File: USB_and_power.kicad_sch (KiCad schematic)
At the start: 48 parts, among them J5 USB_C_Receptacle_USB2.0_14P, SW1 ResetButton, U3 LM2594M-3.3, U4 FT4232H, U5 93LC54B, Y1 ABLS7M2-12.000MHZ-D2Y-T

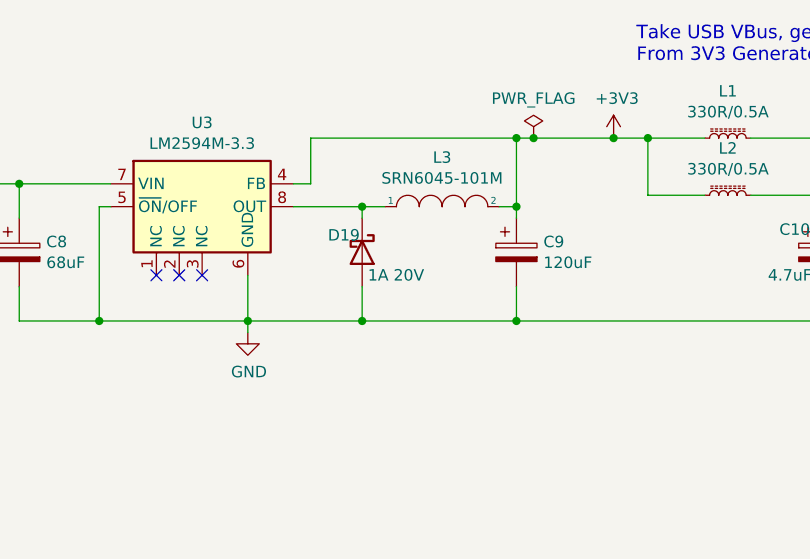
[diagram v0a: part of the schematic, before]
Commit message: BOM updates. Things needed changing due to availability
Tant Caps
Schotkey diodes
Pushbutton Switch

Signed-off-by: Marc Kelly <mpkelly@achenar.co.uk>
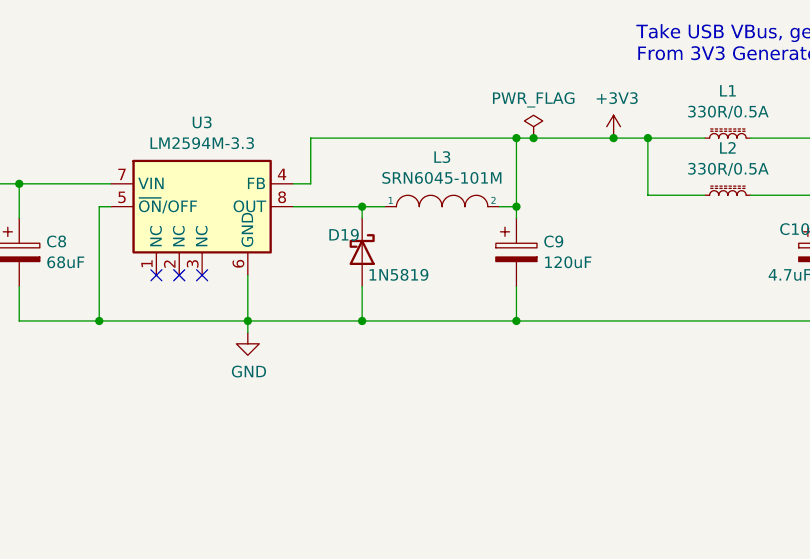
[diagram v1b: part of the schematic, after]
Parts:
- C10, C12: MFN Kyocera AVX -> Murata; MFP F981C475MMA -> GRM188R61E475KE11D; SUPPLIER_LINK https://www.mouser.co.uk/ProductDetail/Kyocera-AVX/F981C475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 -> https://eu.mouser.com/ProductDetail/Murata-Electronics/GRM1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; SUPPLIER_PN 647-F981C475MMA -> 81-GRM188R61E475KE1D
- D19: value 1A 20V -> 1N5819; MFN MCC -> Diodes Inc; MFP MBRX120LF-TP -> 1N5819HW-7-F; SUPPLIER_LINK https://www.mouser.co.uk/ProductDetail/Micro-Commercial-Com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 -> (none); SUPPLIER_PN 833-MBRX120LF-TP -> 621-1N5819HW-F
- SW1: SUPPLIER Farnell -> Mouser; SUPPLIER_PN 4715649 -> 640-SWT0110020016SSA
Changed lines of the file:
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@@
 			)
 		)
-		(property "Value" "1A 20V"
+		(property "Value" "1N5819"
 			(at 122.555 96.393 90)
 			(show_name no)
@@
 			)
 		)
-		(property "Datasheet" ""
+		(property "Datasheet" "https://4donline.ihs.com/images/VipMasterIC/IC/DIOD/DIOD-S-A0011437026/DIOD-S-A0011683586-1.pdf?hkey=CECEF36DEECDED6468708AAF2E19C0C6"
 			(at 121.92 93.853 0)
 			(hide yes)
@@
 			)
 		)
-		(property "MFN" "MCC"
+		(property "MFN" "Diodes Inc"
 			(at 121.92 93.853 0)
 			(hide yes)
@@
 			)
 		)
-		(property "MFP" "MBRX120LF-TP"
+		(property "MFP" "1N5819HW-7-F"
 			(at 121.92 93.853 0)
 			(hide yes)
@@
 			)
 		)
-		(property "SUPPLIER_LINK" "https://www.mouser.co.uk/ProductDetail/Micro-Commercial-Components-MCC/MBRX120LF-TP?qs=SdqRYZZ9IxC6ZMQgVhMv%2FA%3D%3D"
+		(property "SUPPLIER_PN" "621-1N5819HW-F"
+			(at 121.92 93.853 0)
+			(hide yes)
+			(show_name no)
+			(do_not_autoplace no)
+			(effects
+				(font
+					(size 1.27 1.27)
+				)
+			)
+		)
+		(property "ALT_SUPPLIER" ""
 			(at 121.92 93.853 0)
 			(hide yes)
@@
 			)
 		)
-		(property "SUPPLIER_PN" "833-MBRX120LF-TP"
+		(property "ALT_SUPPLIER_PN" ""
+			(at 121.92 93.853 0)
+			(hide yes)
+			(show_name no)
+			(do_not_autoplace no)
+			(effects
+				(font
+					(size 1.27 1.27)
+				)
+			)
+		)
+		(property "ALT_SUPPLIER_LINK" ""
+			(at 121.92 93.853 0)
+			(hide yes)
+			(show_name no)
+			(do_not_autoplace no)
+			(effects
+				(font
+					(size 1.27 1.27)
+				)
+			)
+		)
+		(property "SUPPLIER_LINK" ""
 			(at 121.92 93.853 0)
 			(hide yes)
@@
 			)
 		)
-		(property "Datasheet" ""
+		(property "Datasheet" "https://eu.mouser.com/datasheet/3/76/2/GRM188R61E475KE11_01A.pdf"
 			(at 172.72 93.853 0)
 			(hide yes)
@@
 			)
 		)
-		(property "MFN" "Kyocera AVX"
+		(property "MFN" "Murata"
 			(at 172.72 93.853 0)
 			(hide yes)
@@
 			)
 		)
-		(property "MFP" "F981C475MMA"
+		(property "MFP" "GRM188R61E475KE11D"
 			(at 172.72 93.853 0)
 			(hide yes)
@@
 			)
 		)
-		(property "SUPPLIER_LINK" "https://www.mouser.co.uk/ProductDetail/Kyocera-AVX/F981C475MMA?qs=a5AWWN0nKwZ6rGqyDWG78w%3D%3D"
+		(property "SUPPLIER_LINK" "https://eu.mouser.com/ProductDetail/Murata-Electronics/GRM188R61E475KE11D?qs=eeBpzGFlv%252B9M0HqzMo%2FgYw%3D%3D"
+			(at 172.72 93.853 0)
+			(hide yes)
+			(show_name no)
+			(do_not_autoplace no)
+			(effects
+				(font
+					(size 1.27 1.27)
+				)
+			)
+		)
+		(property "SUPPLIER_PN" "81-GRM188R61E475KE1D"
+			(at 172.72 93.853 0)
+			(hide yes)
+			(show_name no)
+			(do_not_autoplace no)
+			(effects
+				(font
+					(size 1.27 1.27)
+				)
+			)
+		)
+		(property "ALT_SUPPLIER" ""
 			(at 172.72 93.853 0)
 			(hide yes)
@@
 			)
 		)
-		(property "SUPPLIER_PN" "647-F981C475MMA"
+		(property "ALT_SUPPLIER_PN" ""
+			(at 172.72 93.853 0)
+			(hide yes)
+			(show_name no)
+			(do_not_autoplace no)
+			(effects
+				(font
+					(size 1.27 1.27)
+				)
+			)
+		)
+		(property "ALT_SUPPLIER_LINK" ""
 			(at 172.72 93.853 0)
 			(hide yes)
@@
 			)
 		)
-		(property "Datasheet" ""
+		(property "Datasheet" "https://eu.mouser.com/datasheet/3/76/2/GRM188R61E475KE11_01A.pdf"
 			(at 191.77 93.853 0)
 			(hide yes)
@@
 			)
 		)
-		(property "MFN" "Kyocera AVX"
+		(property "MFN" "Murata"
 			(at 191.77 93.853 0)
 			(hide yes)
@@
 			)
 		)
-		(property "MFP" "F981C475MMA"
+		(property "MFP" "GRM188R61E475KE11D"
 			(at 191.77 93.853 0)
 			(hide yes)
@@
 			)
 		)
-		(property "SUPPLIER_LINK" "https://www.mouser.co.uk/ProductDetail/Kyocera-AVX/F981C475MMA?qs=a5AWWN0nKwZ6rGqyDWG78w%3D%3D"
+		(property "SUPPLIER_LINK" "https://eu.mouser.com/ProductDetail/Murata-Electronics/GRM188R61E475KE11D?qs=eeBpzGFlv%252B9M0HqzMo%2FgYw%3D%3D"
 			(at 191.77 93.853 0)
 			(hide yes)
@@
 			)
 		)
-		(property "SUPPLIER_PN" "647-F981C475MMA"
+		(property "SUPPLIER_PN" "81-GRM188R61E475KE1D"
+			(at 191.77 93.853 0)
+			(hide yes)
+			(show_name no)
+			(do_not_autoplace no)
+			(effects
+				(font
+					(size 1.27 1.27)
+				)
+			)
+		)
+		(property "ALT_SUPPLIER" ""
+			(at 191.77 93.853 0)
+			(hide yes)
+			(show_name no)
+			(do_not_autoplace no)
+			(effects
+				(font
+					(size 1.27 1.27)
+				)
+			)
+		)
+		(property "ALT_SUPPLIER_PN" ""
+			(at 191.77 93.853 0)
+			(hide yes)
+			(show_name no)
+			(do_not_autoplace no)
+			(effects
+				(font
+					(size 1.27 1.27)
+				)
+			)
+		)
+		(property "ALT_SUPPLIER_LINK" ""
 			(at 191.77 93.853 0)
 			(hide yes)
@@
 			)
 		)
-		(property "SUPPLIER" "Farnell"
+		(property "SUPPLIER" "Mouser"
 			(at 198.12 164.084 0)
 			(hide yes)
@@
 			)
 		)
-		(property "SUPPLIER_PN" "4715649"
+		(property "SUPPLIER_PN" "640-SWT0110020016SSA"
 			(at 198.12 164.084 0)
 			(hide yes)

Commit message: Adding some Alt suppliers for suppler pns
Signed-off-by: Marc Kelly <mpkelly@achenar.co.uk>
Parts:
- C1, C11, C13, C15, C17, C18, C19, C2, C20, C3, C4, C5, C6, C7: ALT_SUPPLIER (none) -> DigiKey; ALT_SUPPLIER_PN (none) -> 399-C0603C104J4RACTUCT-ND
- C10, C12: ALT_SUPPLIER (none) -> DigiKey; ALT_SUPPLIER_PN (none) -> 490-7203-1-ND
- C14: ALT_SUPPLIER (none) -> DigiKey; ALT_SUPPLIER_PN (none) -> 399-C0603C103J3RACAUTOCT-ND
- C16: ALT_SUPPLIER (none) -> DigiKey; ALT_SUPPLIER_PN (none) -> 478-4949-1-ND
- C8: ALT_SUPPLIER (none) -> DigiKey; ALT_SUPPLIER_PN (none) -> 478-3069-1-ND
- C9: ALT_SUPPLIER (none) -> DigiKey; ALT_SUPPLIER_PN (none) -> 10-EEE-FN1A151LCT-ND
- D19: ALT_SUPPLIER (none) -> DigiKey; ALT_SUPPLIER_PN (none) -> 1N5819HW-FDICT-ND
- D20, D23: ALT_SUPPLIER (none) -> DigiKey; ALT_SUPPLIER_PN (none) -> ESD5Z2.5T1GOSCT-ND
- D21: ALT_SUPPLIER (none) -> DigiKey; ALT_SUPPLIER_PN (none) -> 732-155060GS75300CT-ND
- D22: ALT_SUPPLIER (none) -> DigiKey; ALT_SUPPLIER_PN (none) -> 732-12014-1-ND
- F1: ALT_SUPPLIER (none) -> DigiKey; ALT_SUPPLIER_PN (none) -> 5923-0ZCJ0075AF2ECT-ND
- J5: ALT_SUPPLIER (none) -> DigiKey; ALT_SUPPLIER_PN (none) -> 2223-UJ20-C-H-G-SMT-2A-P16-TRCT-ND
- L1, L2, L4: ALT_SUPPLIER (none) -> DigiKey; ALT_SUPPLIER_PN (none) -> 445-175372-1-ND
- L3: ALT_SUPPLIER (none) -> DigiKey; ALT_SUPPLIER_PN (none) -> SRN6045-101MCT-ND
- R17, R18: ALT_SUPPLIER (none) -> DigiKey; ALT_SUPPLIER_PN (none) -> RMCF0603FT10R0
- R19, R24: ALT_SUPPLIER (none) -> DigiKey; ALT_SUPPLIER_PN (none) -> RC0603FR-0710KL
- R20: ALT_SUPPLIER (none) -> DigiKey; ALT_SUPPLIER_PN (none) -> RC0402FR-0712KL
- R21, R28: ALT_SUPPLIER (none) -> DigiKey; ALT_SUPPLIER_PN (none) -> CAS06F0000CT
- R22, R23: ALT_SUPPLIER (none) -> DigiKey; ALT_SUPPLIER_PN (none) -> RC0603FR-075K1L
- R25: ALT_SUPPLIER (none) -> DigiKey; ALT_SUPPLIER_PN (none) -> YAG3590CT-ND
- R26, R27: ALT_SUPPLIER (none) -> DigiKey; ALT_SUPPLIER_PN (none) -> RC0603FR-07330RL
- SW1: ALT_SUPPLIER (none) -> DigiKey; ALT_SUPPLIER_PN (none) -> 2073-SWT0110-020016SSACT-ND
- U3: ALT_SUPPLIER (none) -> DigiKey; ALT_SUPPLIER_PN (none) -> LM2594M-3.3/NOPB-ND
- U5: ALT_SUPPLIER (none) -> DigiKey; ALT_SUPPLIER_PN (none) -> 93LC56B-I/MS-ND
- Y1: ALT_SUPPLIER (none) -> DigiKey; ALT_SUPPLIER_PN (none) -> 541-XT9MNLANA14M31818-ND
